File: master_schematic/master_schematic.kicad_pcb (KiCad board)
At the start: 4 copper layers, 157.5 x 111.9 mm, 84 parts, among them J1 12V Female, J10 0430450400, J11 1723103102, J12 1723103102, J13 1723103102, J14 1723103102, J15 1723103102, J16 1723103102, J17 1723103102, J18 1723103102, J19 1723103102, J2 0430450400, J20 1723103102, J21 5V Female, J3 0430450400, J4 0430450400, J5 0430450400, J6 0430450400, J7 0430450400, J8 0430450400, J9 0430450400, Q1 CWDM3011N TR13 PBFREE, Q10 CWDM3011N TR13 PBFREE, Q2 CWDM3011N TR13 PBFREE, Q3 CWDM3011N TR13 PBFREE, Q4 CWDM3011N TR13 PBFREE, Q5 CWDM3011N TR13 PBFREE, Q6 CWDM3011N TR13 PBFREE, Q7 CWDM3011N TR13 PBFREE, Q8 CWDM3011N TR13 PBFREE, Q9 CWDM3011N TR13 PBFREE, SW1 SW_SPST, U1 RFM95, U10 HX711, U11 HX711, U2 teensy_4.1, U4 MCP9600_Module, U5 MCP9600_Module, U6 MCP9600_Module, U7 MCP9600_Module, U8 MCP9600_Module, U9 HX711

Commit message: I dont know what change this is lol
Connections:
- U2 pad 5V: +5V -> (no net)
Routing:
- net /PV1_T: track 7.20 -> 100.3 mm, vias 1 -> 4
- net /SDA: track 76.5 -> 145.8 mm
- net /SCL: track 91.5 -> 134.6 mm
- net Net-(D10-A): track 0.00 -> 40.2 mm
- net Net-(D9-A): track 0.00 -> 37.4 mm
- net Net-(D8-A): track 0.00 -> 35.0 mm
- net +12V: track 0.00 -> 32.4 mm, vias 0 -> 10
- net Net-(D7-A): track 0.00 -> 31.9 mm
- net Net-(D6-A): track 0.00 -> 29.2 mm
- net /PT1_T: track 32.1 -> 60.4 mm, vias 0 -> 1
- net Net-(D5-A): track 0.01 -> 27.4 mm
- net Net-(D1-A): track 0.00 -> 25.2 mm
- net Net-(D4-A): track 0.00 -> 25.0 mm
- net Net-(D2-A): track 0.00 -> 24.2 mm
- net Net-(D3-A): track 0.00 -> 23.7 mm
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
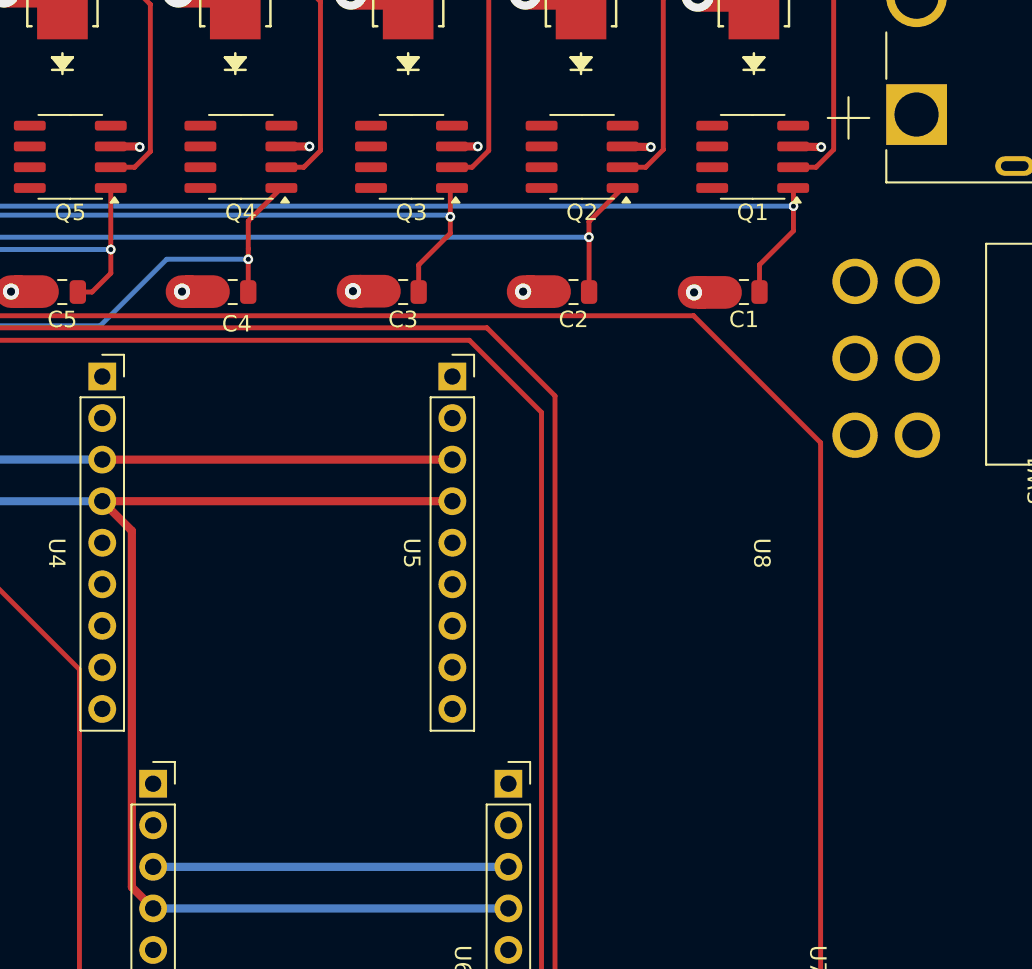
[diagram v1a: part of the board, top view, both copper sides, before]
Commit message: Edited the switch to be in series with the circuit (instead of parallel)
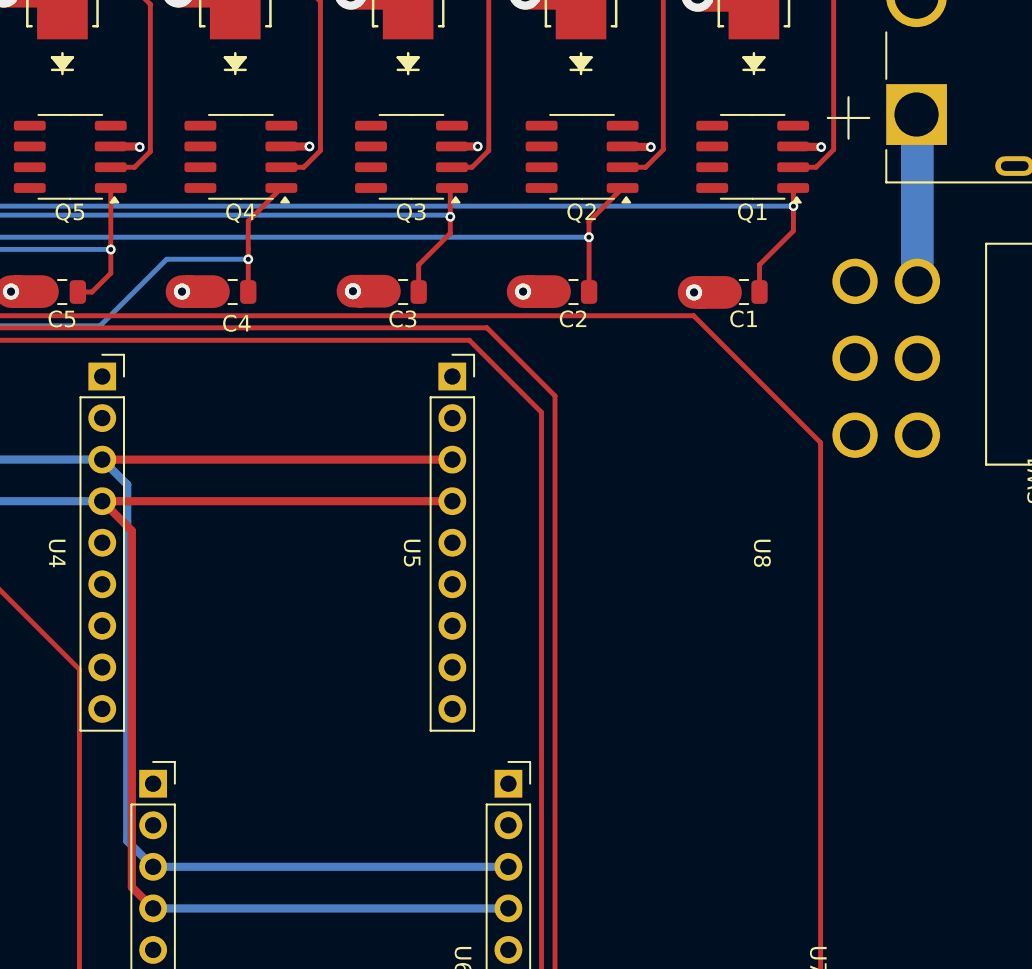
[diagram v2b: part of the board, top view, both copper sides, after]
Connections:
- J1 pad 1: +12V -> Net-(J1-Pin_1)
- SW1 pad 1: Net-(SW1-A) -> Net-(J1-Pin_1)
- U2 pad 5V: (no net) -> +5V
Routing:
- net /SCL: track 134.6 -> 160.8 mm
- net Net-(J1-Pin_1): track 0.00 -> 10.2 mm
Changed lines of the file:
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@@
 	(net 114 "unconnected-(U2-PadLED)")
 	(net 115 "unconnected-(U2-PadVUSB)")
-	(net 116 "Net-(SW1-A)")
+	(net 116 "Net-(J1-Pin_1)")
 	(net 117 "unconnected-(U4-ADDR-Pad9)")
 	(net 118 "unconnected-(U5-ADDR-Pad9)")
@@
 			(layers "*.Cu" "*.Mask")
 			(remove_unused_layers no)
+			(net 14 "+5V")
 			(pinfunction "5V")
 			(pintype "power_in")
@@
 			(layers "*.Cu" "*.Mask")
 			(remove_unused_layers no)
-			(net 1 "+12V")
+			(net 116 "Net-(J1-Pin_1)")
 			(pinfunction "Pin_1")
 			(pintype "passive")
@@
 			(layers "*.Cu" "*.Mask")
 			(remove_unused_layers no)
-			(net 116 "Net-(SW1-A)")
+			(net 116 "Net-(J1-Pin_1)")
 			(pinfunction "A")
 			(pintype "passive")
@@
 	)
 	(segment
+		(start 118.853 96.203)
+		(end 118.853 74.423)
+		(width 0.5)
+		(layer "B.Cu")
+		(net 80)
+	)
+	(segment
+		(start 120.435 97.785)
+		(end 118.853 96.203)
+		(width 0.5)
+		(layer "B.Cu")
+		(net 80)
+	)
+	(segment
 		(start 117.325 72.895)
 		(end 95.625 72.895)
@@
 	)
 	(segment
+		(start 118.853 74.423)
+		(end 117.325 72.895)
+		(width 0.5)
+		(layer "B.Cu")
+		(net 80)
+	)
+	(segment
 		(start 120.435 97.785)
 		(end 142.15 97.785)
@@
 		(net 85)
 	)
+	(segment
+		(start 167.15 62)
+		(end 167.15 51.85)
+		(width 2)
+		(layer "B.Cu")
+		(net 116)
+	)
+	(segment
+		(start 167.15 51.85)
+		(end 167.1 51.8)
+		(width 2)
+		(layer "B.Cu")
+		(net 116)
+	)
 	(zone

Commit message: Edited silkscreens
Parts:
- added SYM1: Logo_Open_Hardware_Large, hb_footprint_lib:ssilogo, F.Cu at (375.4, 123.1)
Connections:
- U2 pad 5V: +5V -> (no net)
- U2 pad VIN: (no net) -> +5V
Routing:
- net /PT5_I: track 158.0 -> 160.0 mm
- net /PT1_N: track 140.0 -> 142.0 mm
- net /PT4_I: track 146.1 -> 148.1 mm
